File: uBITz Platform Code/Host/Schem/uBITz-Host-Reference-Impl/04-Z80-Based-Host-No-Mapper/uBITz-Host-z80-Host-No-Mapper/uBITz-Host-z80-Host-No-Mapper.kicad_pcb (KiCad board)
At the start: 4 copper layers, 84.3 x 100 mm, 24 parts, among them J3 Conn_01x02_Pin, J4 Conn_02x05_Top_Bottom, U11 24LC16BT-I_SN, U2 Z084000xP, U5 ATF1504AS-10AU100, Y1 ACH-14.31818MHZ-EK

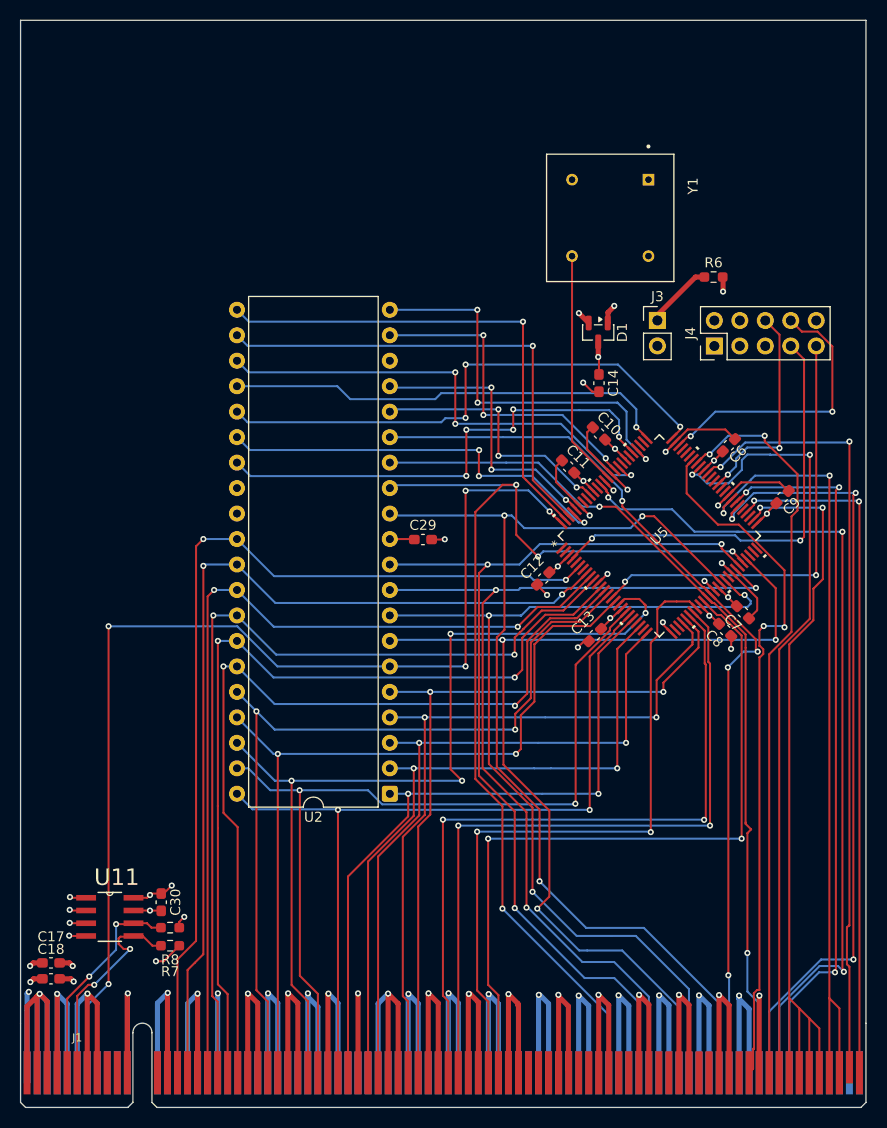
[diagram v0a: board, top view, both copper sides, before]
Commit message: Corrected Bus width (19-bits from 20-bits) and corrected mapper wiring, which needs to be able to re-write bits A13-A15
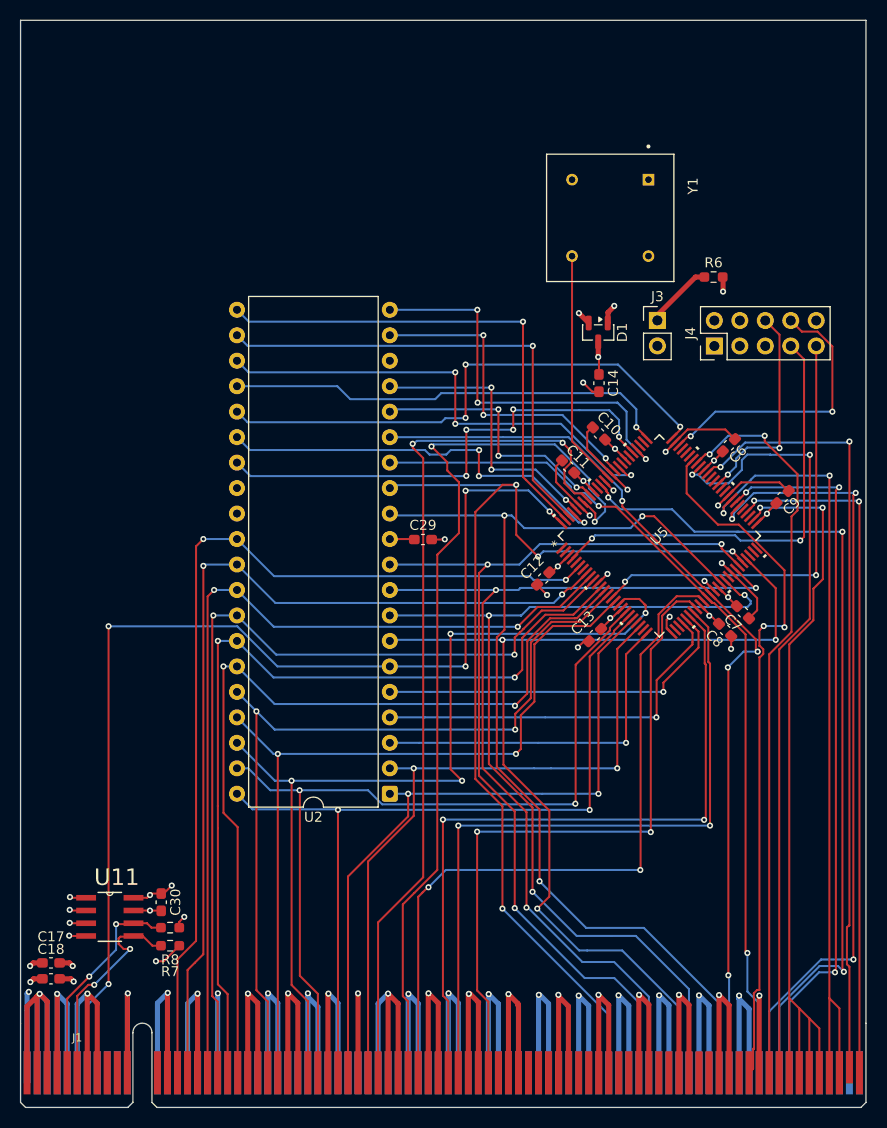
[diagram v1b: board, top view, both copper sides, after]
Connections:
- net /A16 renamed /PA16
- net /A17 renamed /PA17
- net /A18 renamed /PA18
- J1 pad B34: /A13 -> /PA13
- J1 pad B37: /A14 -> /PA14
- J1 pad B38: /A15 -> /PA15
- J1 pad B46: /A19 -> unconnected-(J1A-A19-PadB46)
- U5 pad 35: /A19 -> /PA15
- U5 pad 93: unconnected-(U5-I/O-Pad93) -> /PA13
- U5 pad 94: unconnected-(U5-I/O-Pad94) -> /PA14
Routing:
- net /PA14: track 0.00 -> 91.3 mm, vias 0 -> 2
- net /PA13: track 0.00 -> 87.7 mm, vias 0 -> 2
- net /A19: track 74.5 -> 0.00 mm, vias 2 -> 0
- net /PA15: track 0.00 -> 72.5 mm, vias 0 -> 2
- net /A15: track 75.0 -> 36.5 mm, vias 2 -> 1
- net /A14: track 74.5 -> 37.9 mm, vias 2 -> 1
- net /A13: track 70.0 -> 35.3 mm, vias 2 -> 1
- net /PA18: track 68.9 -> 68.2 mm
- net GND: track 569.7 -> 570.2 mm

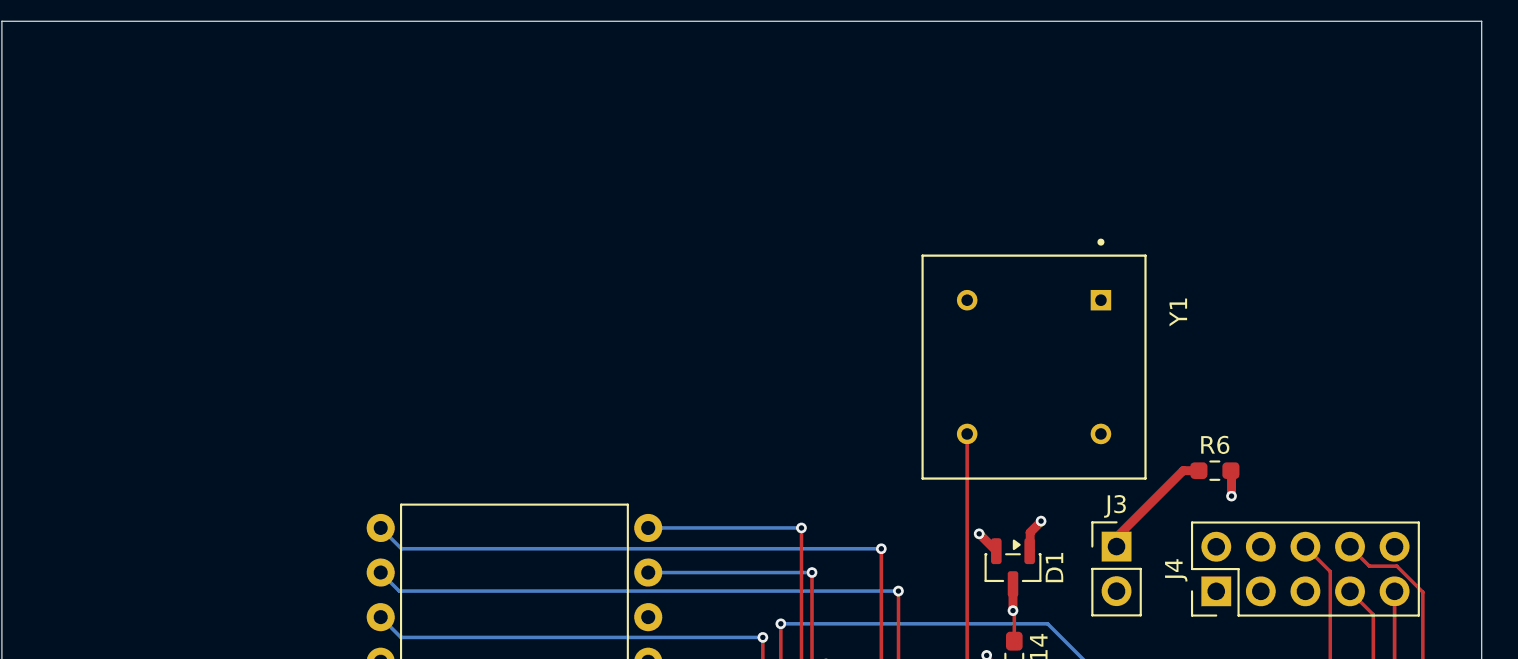
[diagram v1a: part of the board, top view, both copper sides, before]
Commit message: Removed transceivers from Z80 host with the mapper and cleaned up schematics
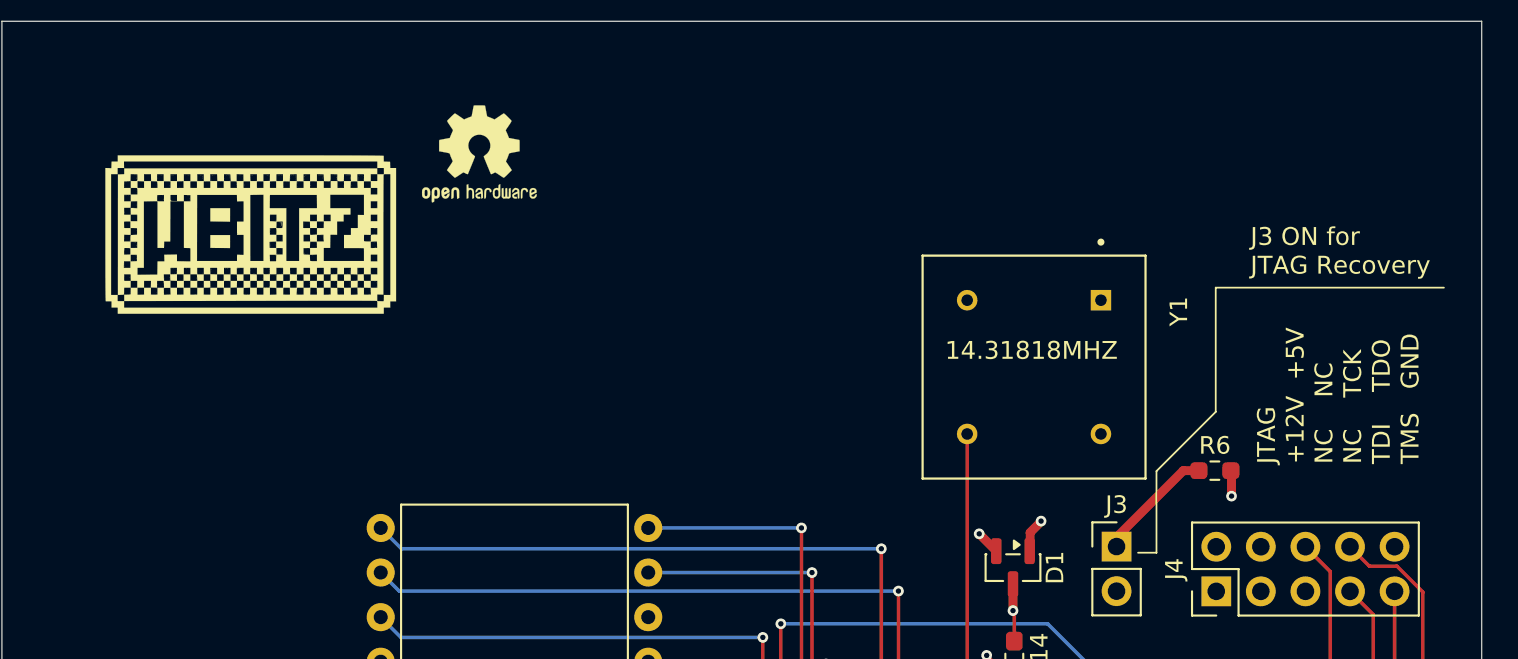
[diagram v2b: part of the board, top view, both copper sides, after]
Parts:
- added G***: LOGO, LOGO, F.Cu at (104.2, 62.3)
- added REF**: OSHW-Logo2_7.3x6mm_SilkScreen, Symbol:OSHW-Logo2_7.3x6mm_SilkScreen, F.Cu at (117.2, 57.6)
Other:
- board text added: "14.31818MHZ"
- board text added: "J3 ON for JTAG Recovery"
- board text added: "JTAG +12V +5V NC NC NC TCK TDI TDO TMS GND"
